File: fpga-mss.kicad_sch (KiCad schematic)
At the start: 7 parts, among them U1 MPFS250T-FCVG484, Y3 Oscillator_125MHz_DSC1103DI2

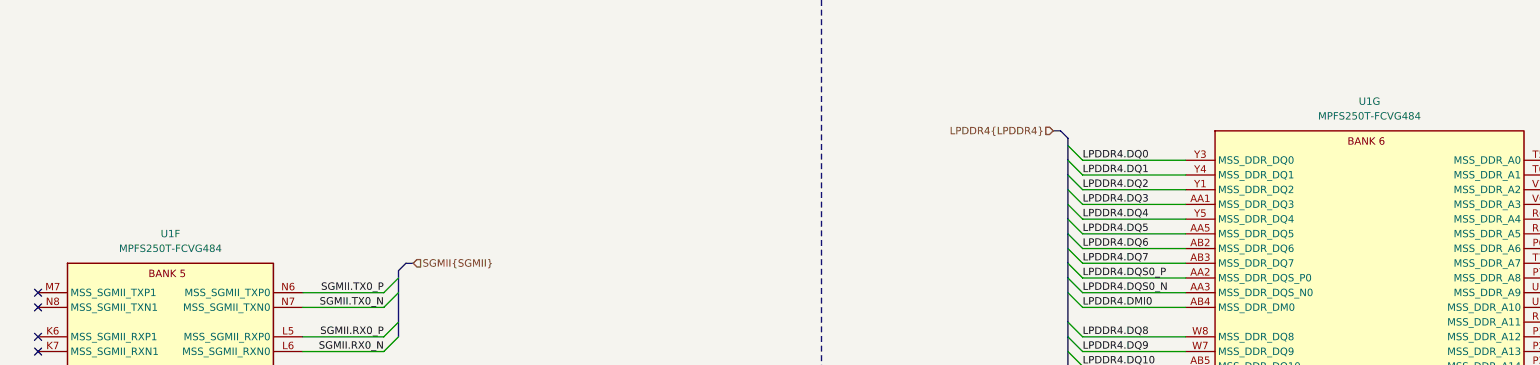
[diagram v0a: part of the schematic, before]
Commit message: [#76827] Update PolarFire MPN. Add test points. Modify DEVRST_N sequence. Bump revision
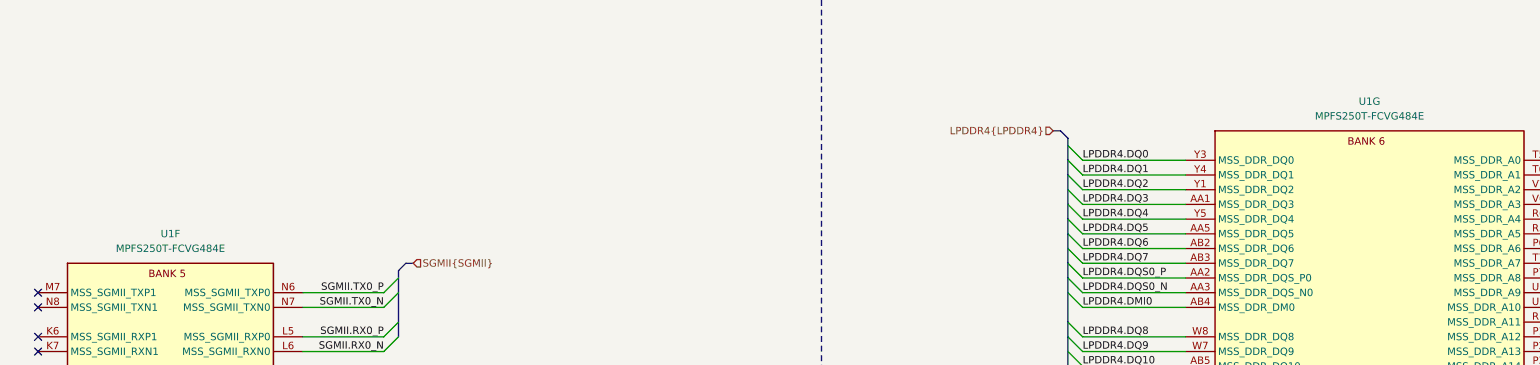
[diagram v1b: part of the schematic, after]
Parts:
- U1: footprint antmicro-footprints:BGA-484_19x19mm_Layout22x22_P0.8mm-microchip-technology-mpfs250t-fcvg484 -> antmicro-footprints:BGA-484_19x19mm_Layout22x22_P0.8mm_FCVG484; symbol antmicroFPGAChips:MPFS250T-FCVG484 -> antmicroFPGAChips:MPFS250T-FCVG484E; MPN MPFS250T-FCVG484 -> MPFS250T-FCVG484E
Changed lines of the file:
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@@
 	(title_block
 		(title "PolarFire SoM")
-		(date "2025-03-25")
-		(rev "1.1.2")
+		(date "2025-04-30")
+		(rev "1.1.3")
 		(company "Antmicro Ltd")
 		(comment 1 "www.antmicro.com")
@@
 	)
 	(symbol
-		(lib_id "antmicroFPGAChips:MPFS250T-FCVG484")
+		(lib_id "antmicroFPGAChips:MPFS250T-FCVG484E")
 		(at 74.93 100.33 0)
 		(unit 6)
@@
 			)
 		)
-		(property "Footprint" "antmicro-footprints:BGA-484_19x19mm_Layout22x22_P0.8mm-microchip-technology-mpfs250t-fcvg484"
+		(property "Footprint" "antmicro-footprints:BGA-484_19x19mm_Layout22x22_P0.8mm_FCVG484"
 			(at 180.34 107.95 0)
 			(effects
@@
 			)
 		)
-		(property "Datasheet" "https://www.microsemi.com/document-portal/doc_download/1244583-polarfire-soc-advance-datasheet"
+		(property "Datasheet" "https://ww1.microchip.com/downloads/aemDocuments/documents/FPGA/ProductDocuments/DataSheets/PolarFire-SoC-Datasheet-DS00004248.pdf"
 			(at 180.34 110.49 0)
 			(effects
@@
 		)
 		(property "Description" "RISC-V System On Chip (SOC) IC PolarFire® FPGA - 254K Logic Modules 484-FCBGA (19x19)"
-			(at 74.93 100.33 0)
+			(at 180.34 120.65 0)
 			(effects
 				(font
 					(size 1.27 1.27)
 				)
+				(justify left bottom)
 				(hide yes)
 			)
 		)
-		(property "MPN" "MPFS250T-FCVG484"
+		(property "MPN" "MPFS250T-FCVG484E"
 			(at 97.79 92.71 0)
 			(effects
@@
 	)
 	(symbol
-		(lib_id "antmicroFPGAChips:MPFS250T-FCVG484")
+		(lib_id "antmicroFPGAChips:MPFS250T-FCVG484E")
 		(at 273.05 77.47 0)
 		(unit 7)
@@
 			)
 		)
-		(property "Footprint" "antmicro-footprints:BGA-484_19x19mm_Layout22x22_P0.8mm-microchip-technology-mpfs250t-fcvg484"
+		(property "Footprint" "antmicro-footprints:BGA-484_19x19mm_Layout22x22_P0.8mm_FCVG484"
 			(at 378.46 85.09 0)
 			(effects
@@
 			)
 		)
-		(property "Datasheet" "https://www.microsemi.com/document-portal/doc_download/1244583-polarfire-soc-advance-datasheet"
+		(property "Datasheet" "https://ww1.microchip.com/downloads/aemDocuments/documents/FPGA/ProductDocuments/DataSheets/PolarFire-SoC-Datasheet-DS00004248.pdf"
 			(at 378.46 87.63 0)
 			(effects
@@
 		)
 		(property "Description" "RISC-V System On Chip (SOC) IC PolarFire® FPGA - 254K Logic Modules 484-FCBGA (19x19)"
-			(at 273.05 77.47 0)
+			(at 378.46 97.79 0)
 			(effects
 				(font
 					(size 1.27 1.27)
 				)
+				(justify left bottom)
 				(hide yes)
 			)
 		)
-		(property "MPN" "MPFS250T-FCVG484"
+		(property "MPN" "MPFS250T-FCVG484E"
 			(at 304.8 69.85 0)
 			(effects
